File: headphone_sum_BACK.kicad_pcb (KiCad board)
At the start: 2 copper layers, 23.1 x 128.5 mm, 44 parts, among them J1 IN_L1, J2 IN_L2, J3 IN_R1, J4 IN_R2, J5 OUT_LR, J6 Eurorack Power, J7 Conn_01x03_Male, J8 Conn_01x02_Female, M3 Screw MountingHole_3.2mm_M3, M3 screw locked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

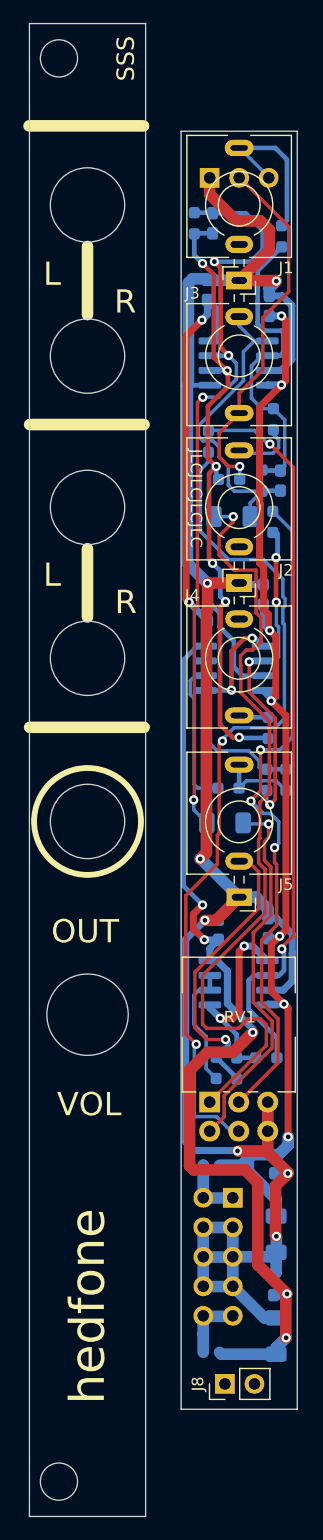
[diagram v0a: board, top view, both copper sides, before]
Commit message: Generate gerbers and BOM for front and back
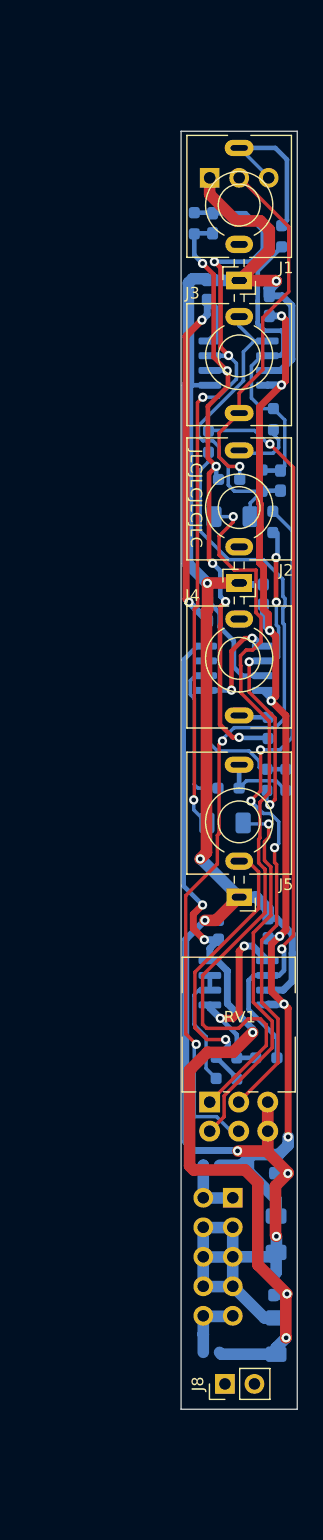
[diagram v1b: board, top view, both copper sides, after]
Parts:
- removed M3 Screw: MountingHole_3.2mm_M3, MountingHole:MountingHole_3.2mm_M3
- removed M3 screw: locked, MountingHole:MountingHole_3.2mm_M3
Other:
- board size 23.1 x 128.5 mm -> 10 x 110 mm
- board text removed: "Front panel"
- board text removed: "Holes with radii larger than 3.15 mm must be made Edge.Cuts, on the 'mechanical' gerber layer (GKO/GML Protel naming). Holes 3.15 mm or smaller radii must be placed as mounting holes (on the drill .drl layer)."
- board text removed: "L"
- board text removed: "Maximum width: 2HP = 9.8 mm 4HP = 20.0 mm 6HP = 30.0 mm 8HP = 40.3 mm 10HP = 50.50 mm 12HP = 60.60 mm Panel height: 128.5 mm Control PCB height: 110mm Consult: http://www.doepfer.de/a100_man/a100m_e.htm"
- board text removed: "OUT"
- board text removed: "R"
- board text removed: "SSS"
- board text removed: "VOL"
- board text removed: "hedfone"
- board text removed: "semi-sensible synth ?"
